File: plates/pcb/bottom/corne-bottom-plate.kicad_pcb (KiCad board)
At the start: 2 copper layers, 133.8 x 91.4 mm, 7 parts

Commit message: Update pcb plates
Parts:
- removed the G*** at (83.6, 115.7)
- removed the G*** at (84.1, 115.7)
- added G***: LOGO, kbd:corne-horizontal, B.Cu at (127.4, 96.5)
- added G***: LOGO, kbd:corne-horizontal, F.Cu at (127.5, 96.5)
- ? (x5): footprint kbd:LEGO_HOLE -> kbd:M2_Hole_TH
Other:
- outline, holes or cut-outs redrawn

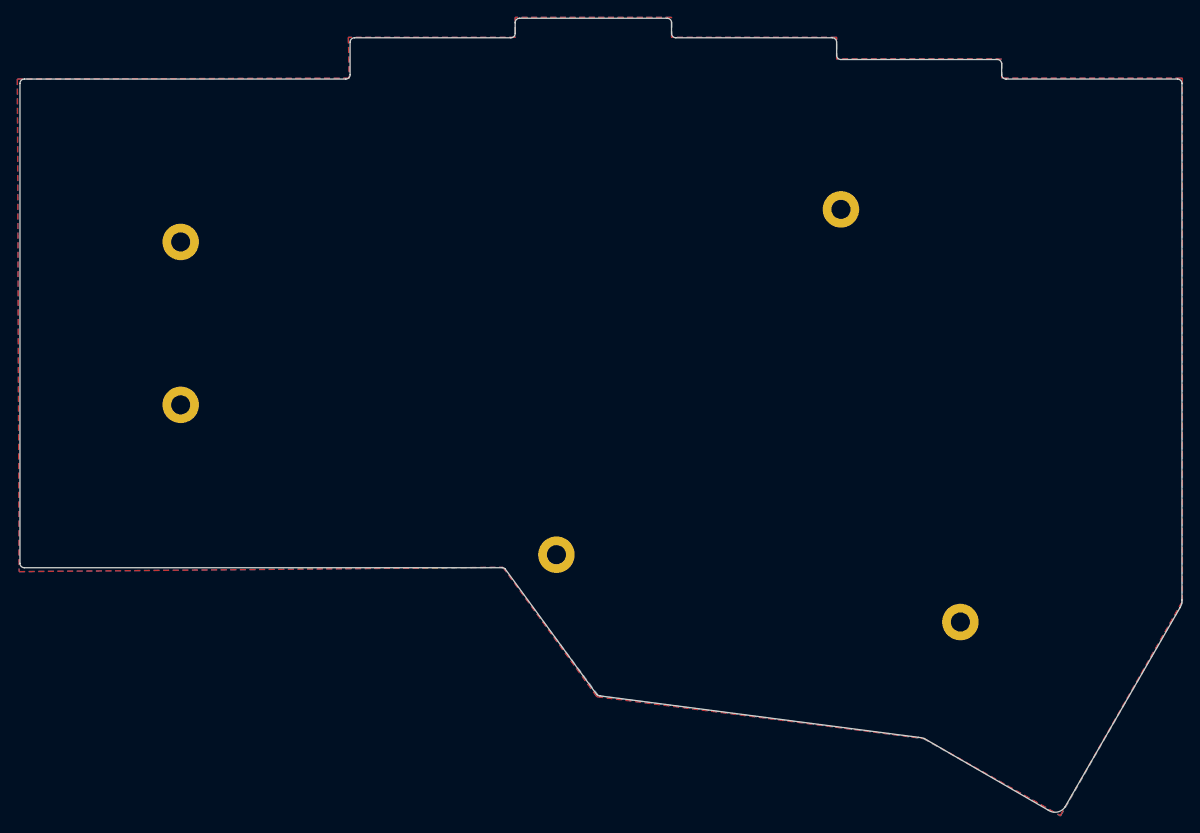
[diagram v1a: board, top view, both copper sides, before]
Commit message: Fix hole size
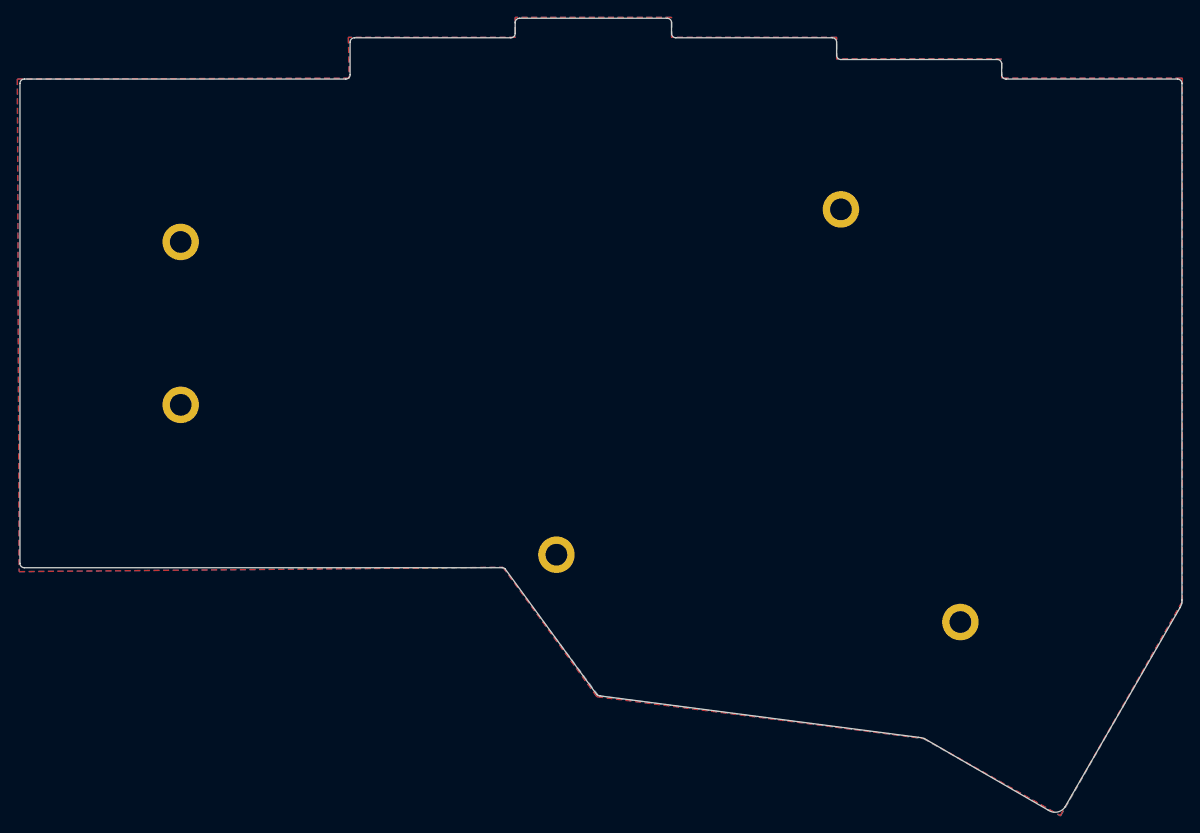
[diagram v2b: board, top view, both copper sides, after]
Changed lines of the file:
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@@
     (uvia_drill 0.1)
+  )
+  (module kbd:M2_Hole_TH (layer F.Cu)
+    (at 79.5 105.5)
+    (fp_text reference "" (at 0 -3.2) (layer F.SilkS)
+      (effects (font (size 1 1) (thickness 0.15)))
+    )
+    (fp_text value "" (at 0 3.2) (layer F.Fab)
+      (effects (font (size 1 1) (thickness 0.15)))
+    )
+    (fp_text user %R (at 0.3 0) (layer F.Fab)
+      (effects (font (size 1 1) (thickness 0.15)))
+    )
+    (pad "" thru_hole circle (at 0 0) (size 4.2 4.2) (drill 2.5) (layers *.Cu *.Mask))
+  )
+  (module kbd:M2_Hole_TH (layer F.Cu)
+    (at 79.5 86.75)
+    (fp_text reference "" (at 0 -3.2) (layer F.SilkS)
+      (effects (font (size 1 1) (thickness 0.15)))
+    )
+    (fp_text value "" (at 0 3.2) (layer F.Fab)
+      (effects (font (size 1 1) (thickness 0.15)))
+    )
+    (fp_text user %R (at 0.3 0) (layer F.Fab)
+      (effects (font (size 1 1) (thickness 0.15)))
+    )
+    (pad "" thru_hole circle (at 0 0) (size 4.2 4.2) (drill 2.5) (layers *.Cu *.Mask))
+  )
+  (module kbd:M2_Hole_TH (layer F.Cu)
+    (at 155.5 83)
+    (fp_text reference "" (at 0 -3.2) (layer F.SilkS)
+      (effects (font (size 1 1) (thickness 0.15)))
+    )
+    (fp_text value "" (at 0 3.2) (layer F.Fab)
+      (effects (font (size 1 1) (thickness 0.15)))
+    )
+    (fp_text user %R (at 0.3 0) (layer F.Fab)
+      (effects (font (size 1 1) (thickness 0.15)))
+    )
+    (pad "" thru_hole circle (at 0 0) (size 4.2 4.2) (drill 2.5) (layers *.Cu *.Mask))
+  )
+  (module kbd:M2_Hole_TH (layer F.Cu)
+    (at 122.75 122.75)
+    (fp_text reference "" (at 0 -3.2) (layer F.SilkS)
+      (effects (font (size 1 1) (thickness 0.15)))
+    )
+    (fp_text value "" (at 0 3.2) (layer F.Fab)
+      (effects (font (size 1 1) (thickness 0.15)))
+    )
+    (fp_text user %R (at 0.3 0) (layer F.Fab)
+      (effects (font (size 1 1) (thickness 0.15)))
+    )
+    (pad "" thru_hole circle (at 0 0) (size 4.2 4.2) (drill 2.5) (layers *.Cu *.Mask))
+  )
+  (module kbd:M2_Hole_TH (layer F.Cu)
+    (at 169.25 130.5)
+    (fp_text reference "" (at 0 -3.2) (layer F.SilkS)
+      (effects (font (size 1 1) (thickness 0.15)))
+    )
+    (fp_text value "" (at 0 3.2) (layer F.Fab)
+      (effects (font (size 1 1) (thickness 0.15)))
+    )
+    (fp_text user %R (at 0.3 0) (layer F.Fab)
+      (effects (font (size 1 1) (thickness 0.15)))
+    )
+    (pad "" thru_hole circle (at 0 0) (size 4.2 4.2) (drill 2.5) (layers *.Cu *.Mask))
   )
   (module kbd:corne-horizontal (layer B.Cu)
@@
       (xy -22.304344 -6.871101) (xy -21.766749 -6.826171)) (layer F.Mask) (width 0.01))
   )
-  (module kbd:M2_Hole_TH (layer F.Cu)
-    (at 79.5 105.5)
-    (fp_text reference "" (at 0 -3.2) (layer F.SilkS)
-      (effects (font (size 1 1) (thickness 0.15)))
-    )
-    (fp_text value "" (at 0 3.2) (layer F.Fab)
-      (effects (font (size 1 1) (thickness 0.15)))
-    )
-    (fp_text user %R (at 0.3 0) (layer F.Fab)
-      (effects (font (size 1 1) (thickness 0.15)))
-    )
-    (pad "" thru_hole circle (at 0 0) (size 4.2 4.2) (drill 2.2) (layers *.Cu *.Mask))
-  )
-  (module kbd:M2_Hole_TH (layer F.Cu)
-    (at 79.5 86.75)
-    (fp_text reference "" (at 0 -3.2) (layer F.SilkS)
-      (effects (font (size 1 1) (thickness 0.15)))
-    )
-    (fp_text value "" (at 0 3.2) (layer F.Fab)
-      (effects (font (size 1 1) (thickness 0.15)))
-    )
-    (fp_text user %R (at 0.3 0) (layer F.Fab)
-      (effects (font (size 1 1) (thickness 0.15)))
-    )
-    (pad "" thru_hole circle (at 0 0) (size 4.2 4.2) (drill 2.2) (layers *.Cu *.Mask))
-  )
-  (module kbd:M2_Hole_TH (layer F.Cu)
-    (at 155.5 83)
-    (fp_text reference "" (at 0 -3.2) (layer F.SilkS)
-      (effects (font (size 1 1) (thickness 0.15)))
-    )
-    (fp_text value "" (at 0 3.2) (layer F.Fab)
-      (effects (font (size 1 1) (thickness 0.15)))
-    )
-    (fp_text user %R (at 0.3 0) (layer F.Fab)
-      (effects (font (size 1 1) (thickness 0.15)))
-    )
-    (pad "" thru_hole circle (at 0 0) (size 4.2 4.2) (drill 2.2) (layers *.Cu *.Mask))
-  )
-  (module kbd:M2_Hole_TH (layer F.Cu)
-    (at 122.75 122.75)
-    (fp_text reference "" (at 0 -3.2) (layer F.SilkS)
-      (effects (font (size 1 1) (thickness 0.15)))
-    )
-    (fp_text value "" (at 0 3.2) (layer F.Fab)
-      (effects (font (size 1 1) (thickness 0.15)))
-    )
-    (fp_text user %R (at 0.3 0) (layer F.Fab)
-      (effects (font (size 1 1) (thickness 0.15)))
-    )
-    (pad "" thru_hole circle (at 0 0) (size 4.2 4.2) (drill 2.2) (layers *.Cu *.Mask))
-  )
-  (module kbd:M2_Hole_TH (layer F.Cu)
-    (at 169.25 130.5)
-    (fp_text reference "" (at 0 -3.2) (layer F.SilkS)
-      (effects (font (size 1 1) (thickness 0.15)))
-    )
-    (fp_text value "" (at 0 3.2) (layer F.Fab)
-      (effects (font (size 1 1) (thickness 0.15)))
-    )
-    (fp_text user %R (at 0.3 0) (layer F.Fab)
-      (effects (font (size 1 1) (thickness 0.15)))
-    )
-    (pad "" thru_hole circle (at 0 0) (size 4.2 4.2) (drill 2.2) (layers *.Cu *.Mask))
-  )
   (gr_line (start 169.25 128.05) (end 169.25 132.950063) (layer F.Fab) (width 0.1))

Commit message: Fix hole size
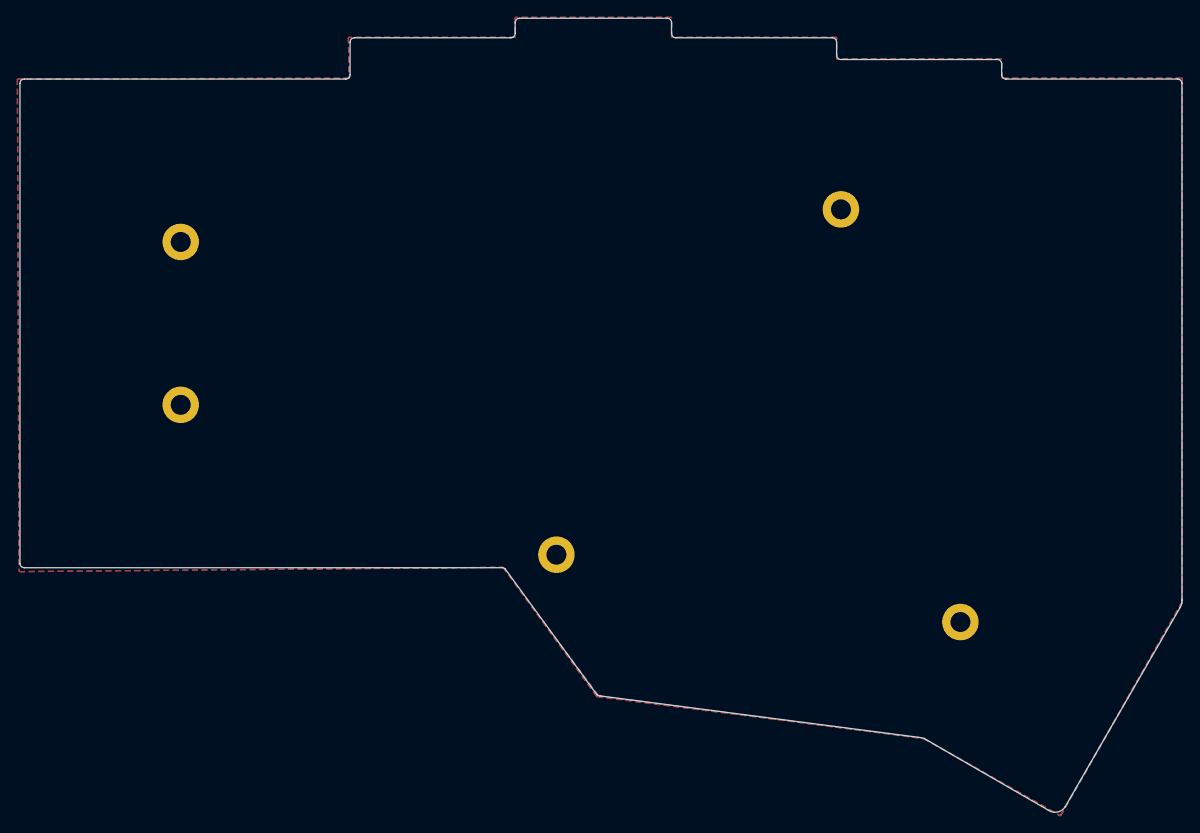
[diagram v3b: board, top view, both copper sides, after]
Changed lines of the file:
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@@
       (effects (font (size 1 1) (thickness 0.15)))
     )
-    (pad "" thru_hole circle (at 0 0) (size 4.2 4.2) (drill 2.5) (layers *.Cu *.Mask))
+    (pad "" thru_hole circle (at 0 0) (size 4.2 4.2) (drill 2.3) (layers *.Cu *.Mask))
   )
   (module kbd:M2_Hole_TH (layer F.Cu)
@@
       (effects (font (size 1 1) (thickness 0.15)))
     )
-    (pad "" thru_hole circle (at 0 0) (size 4.2 4.2) (drill 2.5) (layers *.Cu *.Mask))
+    (pad "" thru_hole circle (at 0 0) (size 4.2 4.2) (drill 2.3) (layers *.Cu *.Mask))
   )
   (module kbd:M2_Hole_TH (layer F.Cu)
@@
       (effects (font (size 1 1) (thickness 0.15)))
     )
-    (pad "" thru_hole circle (at 0 0) (size 4.2 4.2) (drill 2.5) (layers *.Cu *.Mask))
+    (pad "" thru_hole circle (at 0 0) (size 4.2 4.2) (drill 2.3) (layers *.Cu *.Mask))
   )
   (module kbd:M2_Hole_TH (layer F.Cu)
@@
       (effects (font (size 1 1) (thickness 0.15)))
     )
-    (pad "" thru_hole circle (at 0 0) (size 4.2 4.2) (drill 2.5) (layers *.Cu *.Mask))
+    (pad "" thru_hole circle (at 0 0) (size 4.2 4.2) (drill 2.3) (layers *.Cu *.Mask))
   )
   (module kbd:M2_Hole_TH (layer F.Cu)
@@
       (effects (font (size 1 1) (thickness 0.15)))
     )
-    (pad "" thru_hole circle (at 0 0) (size 4.2 4.2) (drill 2.5) (layers *.Cu *.Mask))
+    (pad "" thru_hole circle (at 0 0) (size 4.2 4.2) (drill 2.3) (layers *.Cu *.Mask))
   )
   (module kbd:corne-horizontal (layer B.Cu)

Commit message: plates
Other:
- net class Default removed
